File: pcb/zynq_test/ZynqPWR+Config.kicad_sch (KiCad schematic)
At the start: 43 parts, among them SW501 PS_RST, SW502 PROG, U1 XC7Z020-2CLG400I

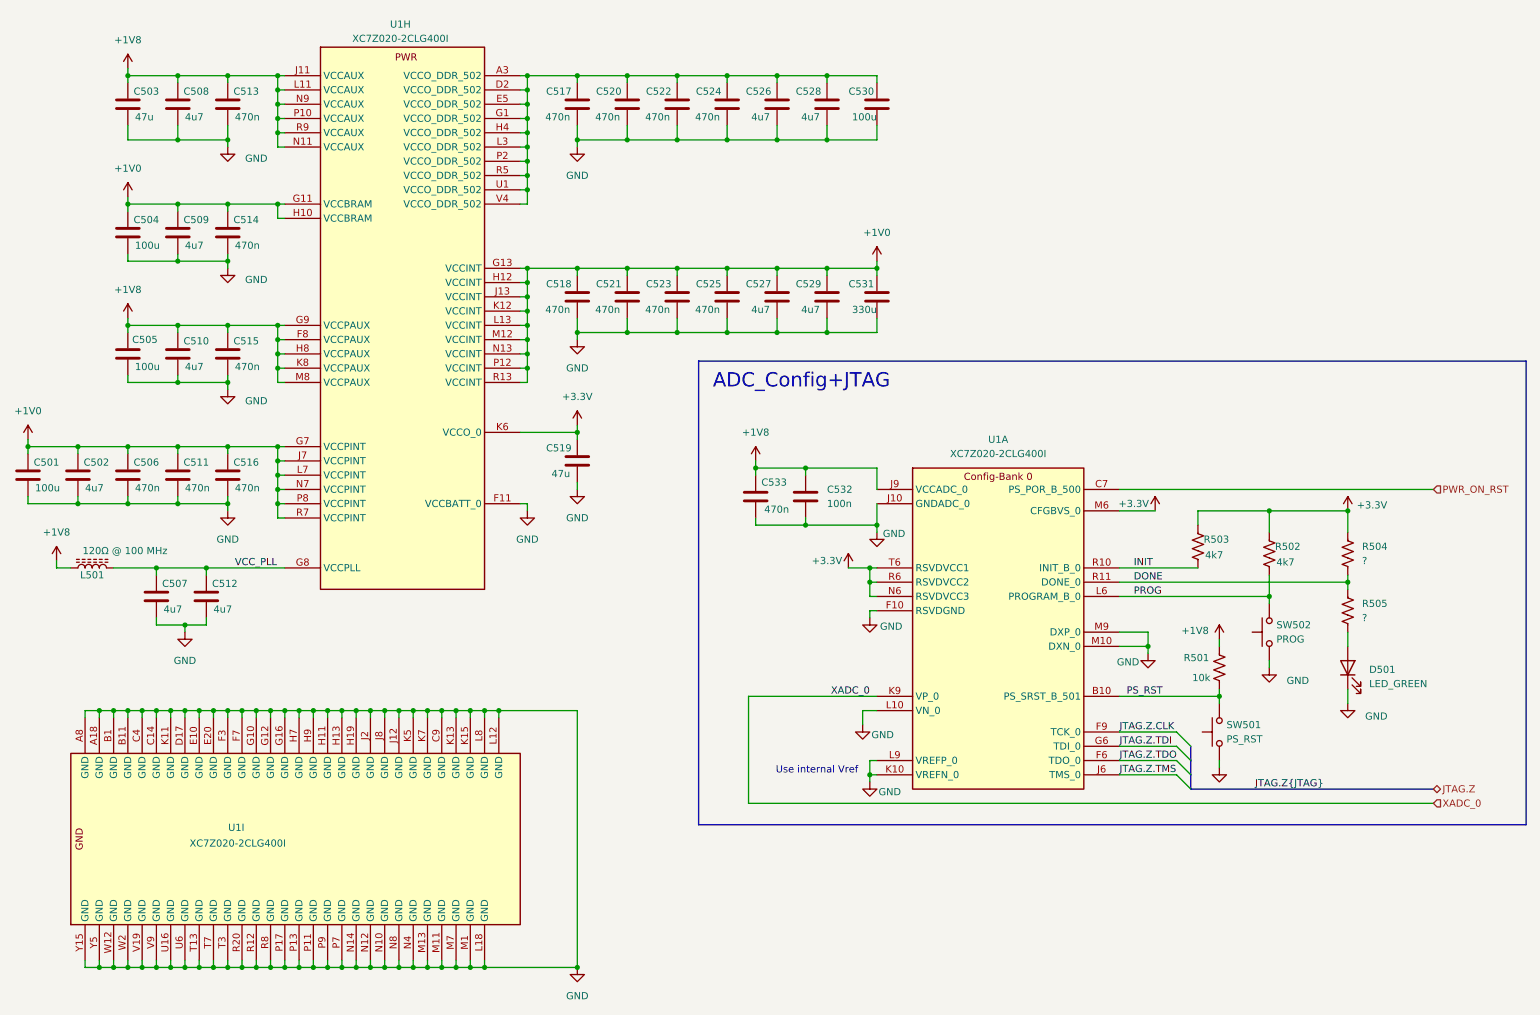
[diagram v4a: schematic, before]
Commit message: Connected DDR3, cleaned up some thing
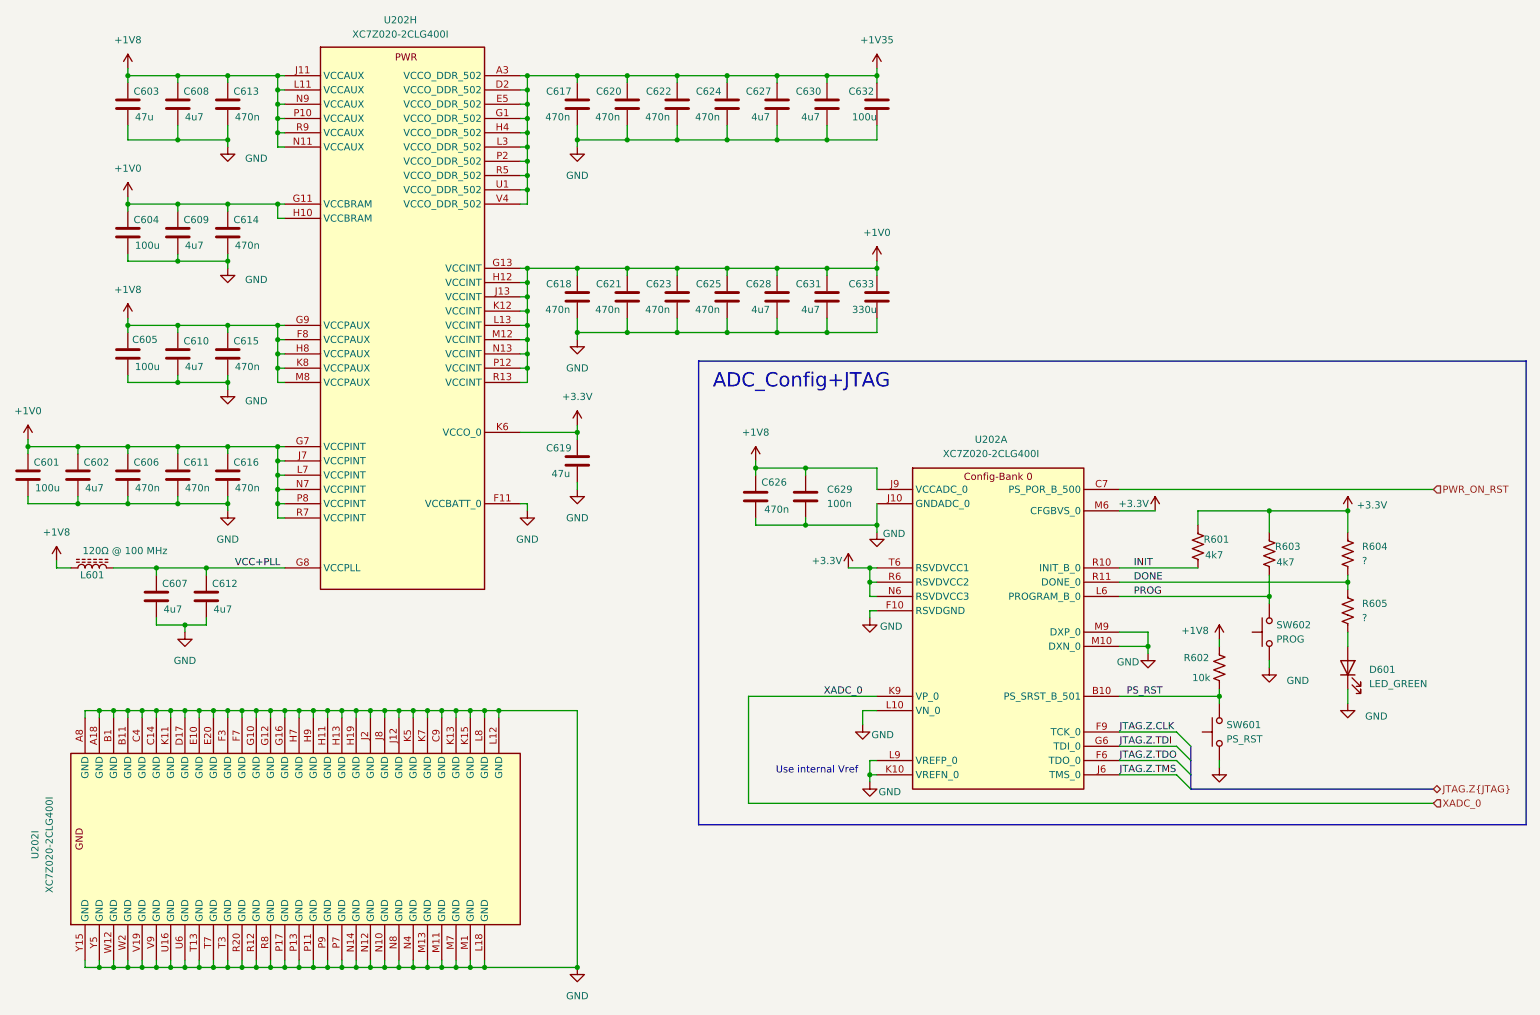
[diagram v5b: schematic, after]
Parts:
- renumbered C501 to C601, C502 to C602, C503 to C603, C504 to C604, C505 to C605, C506 to C606, C507 to C607, C508 to C608, C509 to C609, C510 to C610, C511 to C611, C512 to C612, C513 to C613, C514 to C614, C515 to C615, C516 to C616, C517 to C617, C518 to C618, C519 to C619, C520 to C620, C521 to C621, C522 to C622, C523 to C623, C524 to C624, C525 to C625, C533 to C626, C526 to C627, C527 to C628, C532 to C629, C528 to C630, C529 to C631, C530 to C632, C531 to C633, D501 to D601, L501 to L601, R503 to R601, R501 to R602, R502 to R603, R504 to R604, R505 to R605, SW501 to SW601, SW502 to SW602, U1 to U202
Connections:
- net +1V35: now reaches C617.1, C620.1, C622.1, C624.1, C627.1, C630.1, C632.1, U202.A3 (VCCO_DDR_502), U202.D2 (VCCO_DDR_502), U202.E5 (VCCO_DDR_502), U202.G1 (VCCO_DDR_502), U202.H4 (VCCO_DDR_502), U202.L3 (VCCO_DDR_502), U202.P2 (VCCO_DDR_502), U202.R5 (VCCO_DDR_502), U202.U1 (VCCO_DDR_502), U202.V4 (VCCO_DDR_502)
- net VCC_PLL renamed VCC+PLL

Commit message: Finished Power Supply
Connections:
- net +3.3V renamed +3V3
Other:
- title: (none) -> Zynq Power+Config
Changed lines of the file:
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@@
 	(paper "A4")
 	(title_block
-		(date "2025-09-06")
-		(rev "v1.0")
+		(title "Zynq Power+Config")
+		(date "2025-09-13")
+		(rev "A")
 	)
 	(bus_alias "JTAG"
@@
 			)
 		)
-		(property "Value" "+3.3V"
+		(property "Value" "+3V3"
 			(at 114.3 87.63 0)
 			(effects
@@
 			)
 		)
-		(property "Value" "+3.3V"
+		(property "Value" "+3V3"
 			(at 158.75 116.84 0)
 			(effects
@@
 		(dnp no)
 		(property "Reference" "U202"
-			(at 17.78 167.386 0)
+			(at 57.912 167.386 90)
 			(effects
 				(font
@@
 		)
 		(property "Value" "XC7Z020-2CLG400I"
-			(at 20.32 167.386 0)
+			(at 57.912 164.846 90)
 			(effects
 				(font
@@
 			)
 		)
-		(property "Value" "+3.3V"
+		(property "Value" "+3V3"
 			(at 213.36 106.68 0)
 			(effects
@@
 			)
 		)
-		(property "Value" "+3.3V"
+		(property "Value" "+3V3"
 			(at 255.778 106.934 0)
 			(effects

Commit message: Finished to first ddr ic
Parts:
- U202: footprint Package_BGA:Xilinx_CLG400 -> Zynq:Zynq_Z7020-2CLG400I_W_Delay
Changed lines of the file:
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@@
 			)
 		)
-		(property "Footprint" "Package_BGA:Xilinx_CLG400"
+		(property "Footprint" "Zynq:Zynq_Z7020-2CLG400I_W_Delay"
 			(at 54.61 27.94 0)
 			(effects
@@
 			)
 		)
-		(property "Footprint" "Package_BGA:Xilinx_CLG400"
+		(property "Footprint" "Zynq:Zynq_Z7020-2CLG400I_W_Delay"
 			(at 160.02 53.34 0)
 			(effects
@@
 			)
 		)
-		(property "Footprint" "Package_BGA:Xilinx_CLG400"
+		(property "Footprint" "Zynq:Zynq_Z7020-2CLG400I_W_Delay"
 			(at -22.86 195.58 0)
 			(effects

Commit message: DDR routed
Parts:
- C617, C620, C622, C624, C627, C630, C632: footprint (none) -> Capacitor_SMD:C_0402_1005Metric
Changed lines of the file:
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@@
 			)
 		)
-		(property "Footprint" ""
+		(property "Footprint" "Capacitor_SMD:C_0402_1005Metric"
 			(at 122.2248 39.37 0)
 			(effects
@@
 			)
 		)
-		(property "Footprint" ""
+		(property "Footprint" "Capacitor_SMD:C_0402_1005Metric"
 			(at 140.0048 39.37 0)
 			(effects
@@
 			)
 		)
-		(property "Footprint" ""
+		(property "Footprint" "Capacitor_SMD:C_0402_1005Metric"
 			(at 113.3348 39.37 0)
 			(effects
@@
 			)
 		)
-		(property "Footprint" ""
+		(property "Footprint" "Capacitor_SMD:C_0402_1005Metric"
 			(at 166.6748 39.37 0)
 			(effects
@@
 			)
 		)
-		(property "Footprint" ""
+		(property "Footprint" "Capacitor_SMD:C_0402_1005Metric"
 			(at 131.1148 39.37 0)
 			(effects
@@
 			)
 		)
-		(property "Footprint" ""
+		(property "Footprint" "Capacitor_SMD:C_0402_1005Metric"
 			(at 157.7848 39.37 0)
 			(effects
@@
 			)
 		)
-		(property "Footprint" ""
+		(property "Footprint" "Capacitor_SMD:C_0402_1005Metric"
 			(at 148.8948 39.37 0)
 			(effects
